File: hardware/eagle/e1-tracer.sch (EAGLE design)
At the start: 108 parts, among them IC1 W25Q80DVSNIG, IC2 MCP1703T-1202E/CB, IC3 TPS73633DCQR, IC4 ASEM1-12.000MHZ-LC-T, J1 PASSTHROUGH, M1 MENTOR_12701001, M2 MENTOR_12701001, T1 BC847C, T2 BC847C, U1 ICE40UP5K-SG48I, U2 IP4234CZ6, U3 IDT82V2081, U4 IDT82V2081, U5 2.048 Mhz, U6 1.544 MHz, X1 MINI-USB-SHIELD-UX60-MB-5ST

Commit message: e1-tracer: finish PCB
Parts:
- removed B1: (no value), microbuilder:SWITCH_TACT_SMT
- removed C15: 10n, rc-sysmocom:CAP_CERAMIC_0603
- removed IC3: TPS73633DCQR, laforge:TPS736XX
- removed JP2: TCLK/MCLK, jumper:JP1E
- removed JP3: 1544/2048, jumper:JP2E
- removed R7: 2.2k, rc-sysmocom:RESISTOR_0402
- added IC5: TLV70233DBVR, tlv700xx:TLV70033-SOT
- added R38: 1k, rc-sysmocom:RESISTOR_0603
- added R39, R40, R41: DNP, rc-sysmocom:RESISTOR_0603
- added SW1: TACTSW-TL3340, tact-switches:TL3340
- added U7: 1.544 MHz, laforge:FOX_FXO-HC73
- added X2: JACK2.5_SJ-2523, laforge:JACK2.5_SJ-2523
- C11: value 1u -> 22u; device rc-sysmocom:CAP_CERAMIC_0603 -> rc-sysmocom:CAP_CERAMIC1206; DESCRIPTION CAP CER 1UF 10V X5R 0603 -> CAP CER 22UF 10V 10% X5R 1206; LINK https://www.digikey.de/product-detail/de/samsung-electro-me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 -> http://www.digikey.de/product-detail/de/foo/1276-1287-1-ND; MANUFACTURER Samsung Electro-Mechanics -> Samsung Electro-Mechanics America, Inc; MANUFACTURERPARTNUMBER CL10A105KP8NNNC -> CL31A226KPHNNNE; SOURCEPARTNUMBER 1276-1182-1-ND -> 1276-1287-1-ND
- C12: value 10n -> 1u; device rc-sysmocom:CAP_CERAMIC_0402 -> rc-sysmocom:CAP_CERAMIC_0603; DESCRIPTION CAP CER 10000PF 25V X7R 0402 -> CAP CER 1UF 10V X5R 0603; LINK https://www.digikey.de/product-detail/de/samsung-electro-mechanics/CL05B103KA5NNNC/1276-1057-1-ND/3889143 -> https://www.digikey.de/product-detail/de/samsung-electro-mechanics/CL10A105KP8NNNC/1276-1182-1-ND/3889268; MANUFACTURERPARTNUMBER CL05B103KA5NNNC -> CL10A105KP8NNNC; SOURCEPARTNUMBER 1276-1057-1-ND -> 1276-1182-1-ND
- C13: value 100n -> 10n; device rc-sysmocom:CAP_CERAMIC_0603 -> rc-sysmocom:CAP_CERAMIC_0402; DESCRIPTION CAP CER 0.1UF 16V 10% X7R 0603 -> CAP CER 10000PF 25V X7R 0402; LINK http://www.digikey.de/product-detail/de/foo/1276-1005-1-ND -> https://www.digikey.de/product-detail/de/samsung-electro-me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; MANUFACTURER Samsung Electro-Mechanics America, Inc -> Samsung Electro-Mechanics; MANUFACTURERPARTNUMBER CL10B104KO8NNNC -> CL05B103KA5NNNC; SOURCEPARTNUMBER 1276-1005-1-ND -> 1276-1057-1-ND
- C14: value 22u -> 100n; device rc-sysmocom:CAP_CERAMIC1206 -> rc-sysmocom:CAP_CERAMIC_0603; DESCRIPTION CAP CER 22UF 10V 10% X5R 1206 -> CAP CER 0.1UF 16V 10% X7R 0603; LINK http://www.digikey.de/product-detail/de/foo/1276-1287-1-ND -> http://www.digikey.de/product-detail/de/foo/1276-1005-1-ND; MANUFACTURERPARTNUMBER CL31A226KPHNNNE -> CL10B104KO8NNNC; SOURCEPARTNUMBER 1276-1287-1-ND -> 1276-1005-1-ND
- IC1: value W25Q80DVSNIG -> MCP1703T-1202E/CB; device spiflash:AT25SF-COMB -> MCP170x:MCP1700; DESCRIPTION IC FLASH 8M SPI 104MHZ 8SOIC -> IC REG LIN 1.2V 200MA SOT23A-3; LINK https://www.digikey.de/product-detail/de/winbond-electronic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 -> https://www.digikey.de/product-detail/de/microchip-technolo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; MANUFACTURER Winbond Electronics -> Microchip Technology; MANUFACTURERPARTNUMBER W25Q80DVSNIG -> MCP1703T-1202E/CB; SOURCEPARTNUMBER W25Q80DVSNIG-ND -> MCP1703T-1202E/CBCT-ND
- IC2: value MCP1703T-1202E/CB -> W25Q80DVSNIG; device MCP170x:MCP1700 -> spiflash:AT25SF-COMB; DESCRIPTION IC REG LIN 1.2V 200MA SOT23A-3 -> IC FLASH 8M SPI 104MHZ 8SOIC; LINK https://www.digikey.de/product-detail/de/microchip-technolo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 -> https://www.digikey.de/product-detail/de/winbond-electronic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; MANUFACTURER Microchip Technology -> Winbond Electronics; MANUFACTURERPARTNUMBER MCP1703T-1202E/CB -> W25Q80DVSNIG; SOURCEPARTNUMBER MCP1703T-1202E/CBCT-ND -> W25Q80DVSNIG-ND
- JP1: CLASS (none) -> CONNECTOR\JUMPER; DESCRIPTION (none) -> NO DESCRIPTION; LINK (none) -> UNKNOWN LINK; MANUFACTURER (none) -> UNKNOWN MANUFACTURER; MANUFACTURERPARTNUMBER (none) -> UNKNOWN MANUFACTURER PART NUMBER; POPULATED (none) -> TRUE; ROHSCERTIFICATE (none) -> UNKNOWN ROHS CERTIFICATE; SOURCE (none) -> UNKNOWN SOURCE; SOURCEPARTNUMBER (none) -> UNKNOWN SOURCE PART NUMBER
- LOS1, LOS2: value RED -> LEDPLCC2-MIN-red; device led:LEDCHIPLED_0805 -> LED-PLCC2:LEDPLCC2-MIN; DESCRIPTION NO DESCRIPTION -> LED RED CLEAR 2PLCC SMD; LINK UNKNOWN LINK -> https://www.digikey.de/product-detail/de/osram-opto-semicon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; MANUFACTURER UNKNOWN MANUFACTURER -> OSRAM Opto Semiconductors Inc.; MANUFACTURERPARTNUMBER UNKNOWN MANUFACTURER PART NUMBER -> LS T676-R1S1-1-Z; SOURCE UNKNOWN SOURCE -> DIGIKEY; SOURCEPARTNUMBER UNKNOWN SOURCE PART NUMBER -> 475-2683-1-ND
- M1, M2: CLASS (none) -> UNKNOWN CLASS; DESCRIPTION (none) -> NO DESCRIPTION; LINK (none) -> UNKNOWN LINK; MANUFACTURER (none) -> UNKNOWN MANUFACTURER; MANUFACTURERPARTNUMBER (none) -> UNKNOWN MANUFACTURER PART NUMBER; POPULATED (none) -> TRUE; ROHSCERTIFICATE (none) -> UNKNOWN ROHS CERTIFICATE; SOURCE (none) -> UNKNOWN SOURCE; SOURCEPARTNUMBER (none) -> UNKNOWN SOURCE PART NUMBER
- PWR: value GREEN -> LEDPLCC2-MIN-green; device led:LEDCHIPLED_0805 -> LED-PLCC2:LEDPLCC2-MIN; CLASS UNKNOWN CLASS -> LED; LINK UNKNOWN LINK -> https://www.digikey.de/product-detail/de/rohm-semiconductor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
- R10: value 10k -> 68
- R28: value 3k 1% -> 10k
- R30: value 10k -> 3k 1%
- R32: value 120 -> 10k
- R34: value 68 -> 120
- R35: value 68 -> 330; DESCRIPTION NO DESCRIPTION -> RES SMD 330 OHM 1%% 1/10W 0603; LINK UNKNOWN LINK -> https://www.digikey.de/product-detail/de/yageo/RC0603FR-073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; MANUFACTURER UNKNOWN MANUFACTURER -> Yageo; MANUFACTURERPARTNUMBER UNKNOWN MANUFACTURER PART NUMBER -> RC0603FR-07330RL; SOURCE UNKNOWN SOURCE -> DIGIKEY; SOURCEPARTNUMBER UNKNOWN SOURCE PART NUMBER -> 311-330HRCT-ND
- R36: value 1k -> 330; DESCRIPTION NO DESCRIPTION -> RES SMD 330 OHM 1%% 1/10W 0603; LINK UNKNOWN LINK -> https://www.digikey.de/product-detail/de/yageo/RC0603FR-073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; MANUFACTURER UNKNOWN MANUFACTURER -> Yageo; MANUFACTURERPARTNUMBER UNKNOWN MANUFACTURER PART NUMBER -> RC0603FR-07330RL; SOURCE UNKNOWN SOURCE -> DIGIKEY; SOURCEPARTNUMBER UNKNOWN SOURCE PART NUMBER -> 311-330HRCT-ND
- R8: value 10k -> 2.2k; device rc-sysmocom:RESISTOR_0603 -> rc-sysmocom:RESISTOR_0402; DESCRIPTION RES 10K OHM 1%% 1/10W 0603 -> RES 2.20K OHM 1/16W 1% 0402 SMD; LINK https://www.digikey.de/product-detail/de/stackpole-electron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 -> http://www.digikey.de/product-detail/de/RC0402FR-072K2L/311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; MANUFACTURER Stackpole Electronics Inc -> Yageo; MANUFACTURERPARTNUMBER YPE HTML PUBLIC -> RC0402FR-072K2L; ROHSCERTIFICATE Bleifrei / RoHS3-konform -> Bleifrei / RoHS-konform; SOURCEPARTNUMBER RMCF0603FT10K0CT-ND -> 311-2.20KLRCT-ND
- R9: value 68 -> 10k; DESCRIPTION NO DESCRIPTION -> RES 10K OHM 1%% 1/10W 0603; LINK UNKNOWN LINK -> https://www.digikey.de/product-detail/de/stackpole-electron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; MANUFACTURER UNKNOWN MANUFACTURER -> Stackpole Electronics Inc; MANUFACTURERPARTNUMBER UNKNOWN MANUFACTURER PART NUMBER -> YPE HTML PUBLIC; ROHSCERTIFICATE UNKNOWN ROHS CERTIFICATE -> Bleifrei / RoHS3-konform; SOURCE UNKNOWN SOURCE -> DIGIKEY; SOURCEPARTNUMBER UNKNOWN SOURCE PART NUMBER -> RMCF0603FT10K0CT-ND
- U3: value IDT82V2081 -> IP4234CZ6; device laforge:IDT82V2081 -> laforge:IP4234CZ6; DESCRIPTION NO DESCRIPTION -> TVS DIODE 5.5V 6TSOP; LINK UNKNOWN LINK -> https://www.digikey.de/product-detail/de/nexperia-usa-inc/I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; MANUFACTURER UNKNOWN MANUFACTURER -> Nexperia USA Inc.; MANUFACTURERPARTNUMBER UNKNOWN MANUFACTURER PART NUMBER -> IP4234CZ6,125; ROHSCERTIFICATE UNKNOWN ROHS CERTIFICATE -> Bleifrei / RoHS-konform; SOURCE UNKNOWN SOURCE -> DIGIKEY; SOURCEPARTNUMBER UNKNOWN SOURCE PART NUMBER -> 1727-4717-1-ND
- U5: value 2.048 Mhz -> IDT82V2081; device laforge:FOX_FXO-HC73 -> laforge:IDT82V2081
- U6: value 1.544 MHz -> 2.048 Mhz; MANUFACTURERPARTNUMBER UNKNOWN MANUFACTURER PART NUMBER -> XLH736002.048000I
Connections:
- removed net N$4 (its old number): R28.2, U3G$5.REF
- new net N$1: R30.2, U5G$5.REF
- new net UART_TX0: U3.1A, X2.MIDDLE
- new net VDD: U3.VCC
- net BOOT_SW: now also SW1.2; no longer B1.P, B1.P1
- net CDONE: now also R8.2; no longer R7.2
- net GND: now also IC5.GND, R18.2, R27.2, R30.1, R40.2, R41.1, SW1.1, SW1.3, U3.GND, U5G$3.!RD/DS/SCLKE, U5G$4.JA0, U5G$4.JA1, U5G$4.MODE1, U5G$4.RCLKE, U5G$4.THZ, U5G$5.GNDA, U5G$5.GNDD, U5G$5.GNDIO, U5G$5.GNDT, U7.GND, X2.RING; no longer B1.S, B1.S1, C15.2, IC3.GND, IC3.GND1, JP3.2, R19.2, R28.1, R9.2, U3G$3.!RD/DS/SCLKE, U3G$4.JA0, U3G$4.JA1, U3G$4.MODE1, U3G$4.RCLKE, U3G$4.THZ, U3G$5.GNDA, U3G$5.GNDD, U3G$5.GNDIO, U3G$5.GNDT, U5.GND
- net IOB_32A_SPI_SO: now also IC2.SO(D1); no longer IC1.SO(D1)
- net IOB_33B_SPI_SI: now also IC2.SI(D0); no longer IC1.SI(D0)
- net IOB_34A_SPI_SCK: now also IC2.SCK; no longer IC1.SCK
- net IOB_35B_SPI_SS: now also IC2.!CS; no longer IC1.!CS
- net IO_A0: now also U5G$3.SDI/WR/RW; no longer U3G$3.SDI/WR/RW
- net IO_A1: now also U5G$3.SDO/!ACK/RDY; no longer U3G$3.SDO/!ACK/RDY
- net IO_A2: now also U5G$3.SCLK/ALE/AS; no longer U3G$3.SCLK/ALE/AS
- net IO_A3: now also U3.1B
- net IO_A4: now also U4G$3.!CS; no longer U3G$3.!CS
- net IO_A5: now also U5G$3.!CS; no longer U4G$3.!CS
- net IO_B0: now also U4G$1.RCLK; no longer U3G$1.RCLK
- net IO_B1: now also U4G$1.RD/RDP; no longer U3G$1.RD/RDP
- net IO_B2: now also U5G$1.RCLK; no longer U4G$1.RCLK
- net IO_B3: now also U5G$1.RD/RDP; no longer U4G$1.RD/RDP
- net LOS0: now also R31.2, U4G$1.LOS; no longer R30.2, U3G$1.LOS
- net LOS1: now also R32.2, U5G$1.LOS; no longer R31.2, U4G$1.LOS
- net MCLK: now also R39.2, U5G$6.MCLK, U7.OUT; no longer JP2.1, U3G$6.MCLK, U5.OUT
- net N$10: now also R13.1, U4G$4.PULS1/AD5; no longer R12.1, U3G$4.PULS1/AD5
- net N$11: now also R14.1, U4G$4.PULS0/AD4; no longer R13.1, U3G$4.PULS0/AD4
- net N$12: now also R15.1, U4G$4.EQ/AD3; no longer R14.1, U3G$4.EQ/AD3
- net N$13: now also R16.1, U4G$4.RPD/AD2; no longer R15.1, U3G$4.RPD/AD2
- net N$14: now also R17.1, U4G$4.PATT1/AD1; no longer R16.1, U3G$4.PATT1/AD1
- net N$15: now also R22.1, U5G$4.PULS1/AD5; no longer R21.1, U4G$4.PULS1/AD5
- net N$16: now also R23.1, U5G$4.PULS0/AD4; no longer R22.1, U4G$4.PULS0/AD4
- net N$17: now also R19.1, U4G$4.!RST; no longer R18.1, U3G$4.!RST
- net N$18: now also R18.1, U4G$4.PATT0/AD0; no longer R17.1, U3G$4.PATT0/AD0
- net N$19: now also R24.1, U5G$4.EQ/AD3; no longer R23.1, U4G$4.EQ/AD3
- net N$2: now also R28.1, U5G$4.!RST; no longer R27.1, U4G$4.!RST
- net N$20: now also R25.1, U5G$4.RPD/AD2; no longer R24.1, U4G$4.RPD/AD2
- net N$21: now also R26.1, U5G$4.PATT1/AD1; no longer R25.1, U4G$4.PATT1/AD1
- net N$22: now also R27.1, U5G$4.PATT0/AD0; no longer R26.1, U4G$4.PATT0/AD0
- net N$23: now also U4G$5.VDDA; no longer U3G$5.VDDA
- net N$25: now also R9.1; no longer R8.1
- net N$26: now also R31.1; no longer R30.1
- net N$27: now also R35.1; no longer R34.1
- net N$28: now also R35.2; no longer R34.2
- net N$29: now also R10.1; no longer R9.1
- net N$3: now also U5G$5.VDDA; no longer U4G$5.VDDA
- net N$30: now also R37.1; no longer R36.1
- net N$31: now also R32.1; no longer R31.1
- net N$35: now also R40.1, U6.E/D; no longer JP3.3, U5.E/D
- net N$36: now also X1S.S2, X1S.S3; no longer C15.1, IC3.NR
- net N$37: now also R36.1; no longer R35.1
- net N$38: now also R41.2, U7.E/D; no longer JP3.1, U6.E/D
- net N$39: now also R36.2; no longer R35.2
- net N$41: now also R38.1; no longer R37.1
- net N$42: now also R37.2; no longer R36.2
- net N$5: now also R38.2; no longer R37.2
- net N$6: now also R20.1, U5G$4.PULS3/AD7; no longer R19.1, U4G$4.PULS3/AD7
- net N$61: now also C13.1; no longer C12.1
- net N$7: now also R21.1, U5G$4.PULS2/AD6; no longer R20.1, U4G$4.PULS2/AD6
- net N$8: now also R11.1, U4G$4.PULS3/AD7; no longer R10.1, U3G$4.PULS3/AD7
- net N$9: now also R12.1, U4G$4.PULS2/AD6; no longer R11.1, U3G$4.PULS2/AD6
- net RRING: now also R33.1, U4G$2.RRING; no longer R32.1, U3G$2.RRING
- net RRING1: now also R34.1, U5G$2.RRING; no longer R33.1, U4G$2.RRING
- net RTIP: now also R33.2, U4G$2.RTIP; no longer R32.2, U3G$2.RTIP
- net RTIP1: now also R34.2, U5G$2.RTIP; no longer R33.2, U4G$2.RTIP
- net TCLK: now also R39.1, U5G$1.TCLK; no longer JP2.2, U3G$1.TCLK
- net VBUS: now also C11.1, C12.1, IC1.VIN, IC5.IN; no longer C10.1, C14.1, IC2.VIN, IC3.IN
- net VCC_1V2: now also C10.1, IC1.VO, IC5.EN; no longer C11.1, IC2.VO, IC3.EN
- net VCC_3V3: now also C14.1, IC2.!HOLD(D3), IC2.!WP(D2), IC2.VCC, IC5.OUT, R19.2, R28.2, R8.1, R9.2, U5G$4.MODE0, U5G$5.VDDD, U5G$5.VDDIO, U5G$5.VDDT, U7.VCC; no longer C13.1, IC1.!HOLD(D3), IC1.!WP(D2), IC1.VCC, IC3.OUT, R18.2, R27.2, R7.1, R8.2, U3G$4.MODE0, U3G$5.VDDD, U3G$5.VDDIO, U3G$5.VDDT, U5.VCC
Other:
- note added: "Osmocom-style 3.3V UART on 2.5mm jack"
- note added: "serial debug out"
- moved on the sheet: C10, C11, C12, C13, C14, C16, C29, C9, R11, R12, R13, R14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

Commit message: e1-tracer: reapir missing VDD_3V3 on serial debug out's TVS
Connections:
- removed net VDD: U3.VCC
- net VCC_3V3: now also U3.VCC
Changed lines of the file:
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@@
 </part>
 <part name="GND42" library="supply1" deviceset="GND" device=""/>
-<part name="VDD1" library="supply1" deviceset="VDD" device=""/>
 <part name="IC5" library="tlv700xx" deviceset="TLV700*" device="-SOT" technology="33" value="TLV70233DBVR">
 <attribute name="OC_DIGIKEY" value="296-32415-1-ND"/>
@@
 </instance>
 <instance part="GND42" gate="1" x="314.96" y="193.04"/>
-<instance part="VDD1" gate="G$1" x="314.96" y="226.06"/>
 <instance part="IC5" gate="G$1" x="238.76" y="213.36"/>
 </instances>
@@
 <label x="187.96" y="25.4" size="1.27" layer="95" rot="R90" xref="yes"/>
 </segment>
+<segment>
+<pinref part="U3" gate="G$1" pin="VCC"/>
+<wire x1="314.96" y1="215.9" x2="314.96" y2="218.44" width="0.1524" layer="91"/>
+<label x="314.96" y="218.44" size="1.27" layer="95" rot="R90" xref="yes"/>
+</segment>
 </net>
 <net name="VBUS" class="1">
@@
 </segment>
 </net>
-<net name="VDD" class="2">
-<segment>
-<pinref part="U3" gate="G$1" pin="VCC"/>
-<wire x1="314.96" y1="215.9" x2="314.96" y2="223.52" width="0.1524" layer="91"/>
-<pinref part="VDD1" gate="G$1" pin="VDD"/>
-</segment>
-</net>

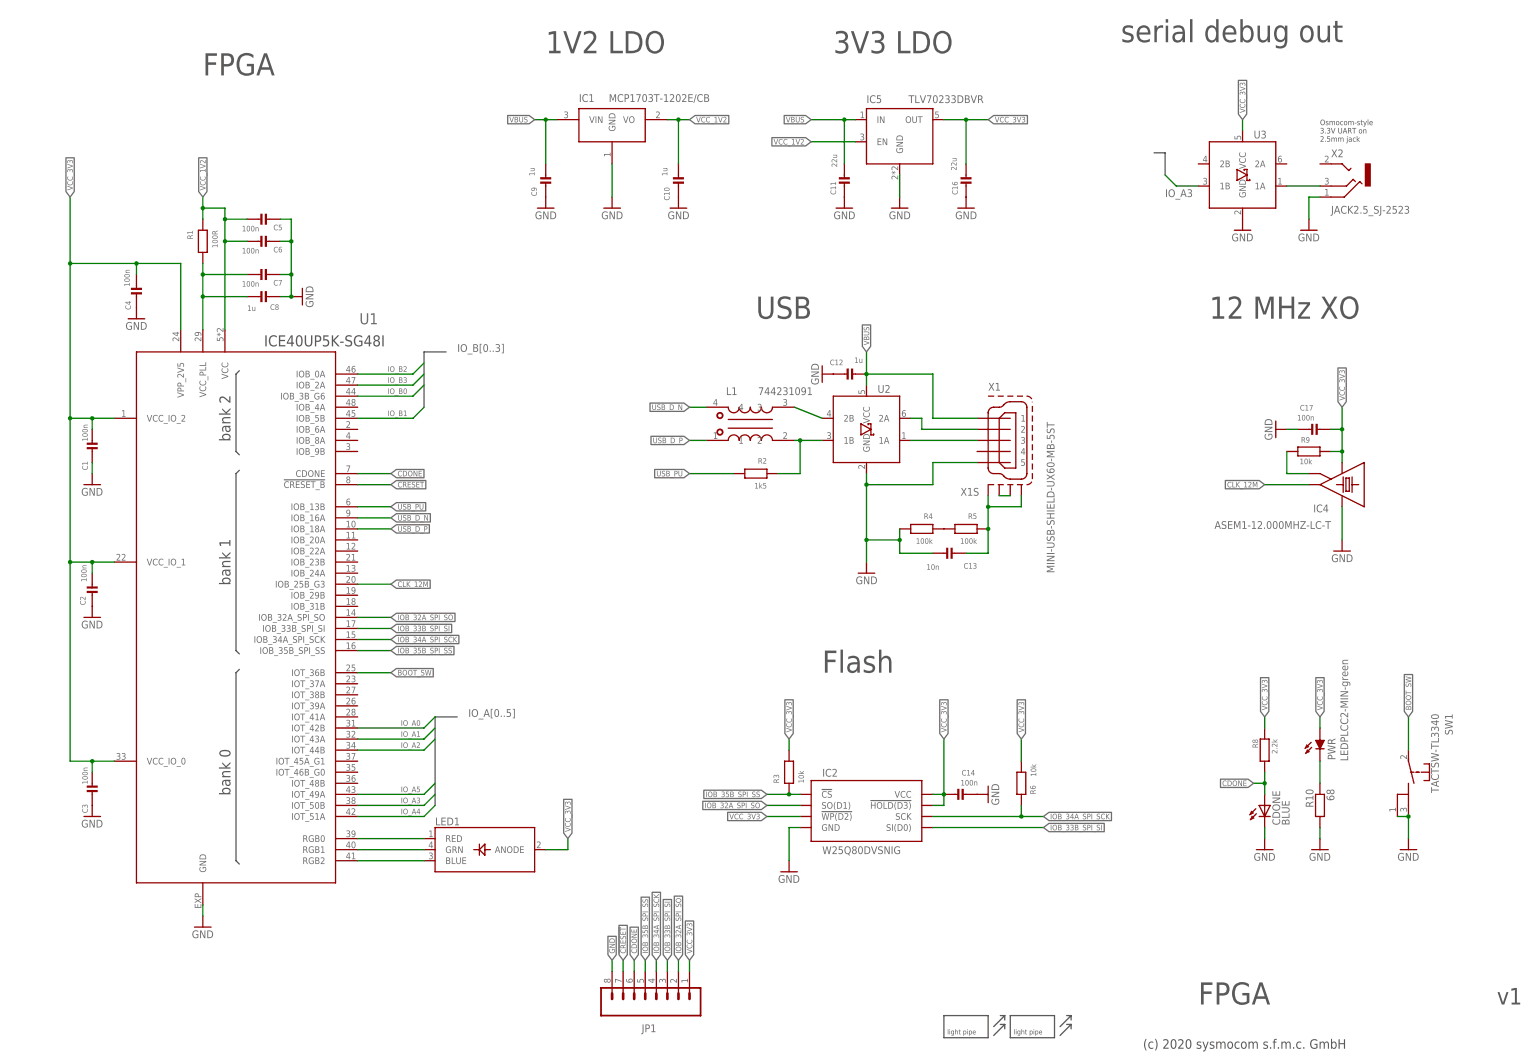
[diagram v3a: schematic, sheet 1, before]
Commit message: e1-tracer: add 2x 33R series resistors in USB wires
and
* update improved HC73 package
* move upper third of PCB (LIUs and XOs) left
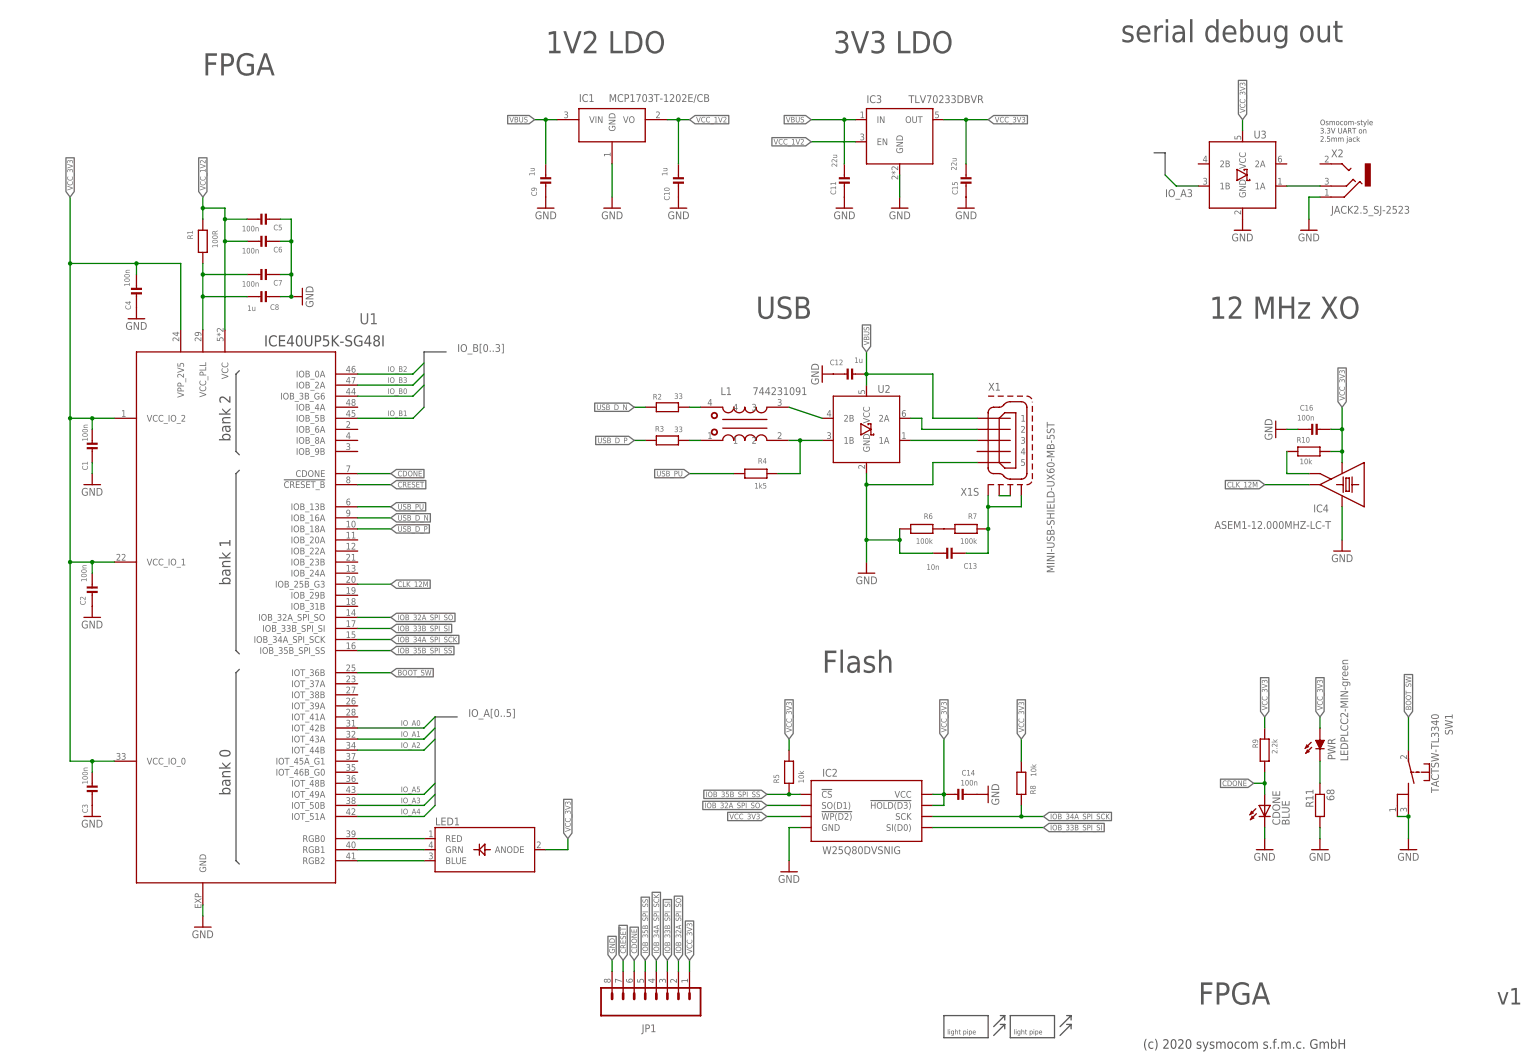
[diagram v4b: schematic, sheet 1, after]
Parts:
- removed C29: 100n, rc-sysmocom:CAP_CERAMIC_0603
- added C15: 22u, rc-sysmocom:CAP_CERAMIC1206
- added R42: DNP, rc-sysmocom:RESISTOR_0603
- added R7: 100k, rc-sysmocom:RESISTOR_0603
- C16: value 22u -> 100n; device rc-sysmocom:CAP_CERAMIC1206 -> rc-sysmocom:CAP_CERAMIC_0603; DESCRIPTION CAP CER 22UF 10V 10% X5R 1206 -> CAP CER 0.1UF 16V 10% X7R 0603; LINK http://www.digikey.de/product-detail/de/foo/1276-1287-1-ND -> http://www.digikey.de/product-detail/de/foo/1276-1005-1-ND; MANUFACTURERPARTNUMBER CL31A226KPHNNNE -> CL10B104KO8NNNC; SOURCEPARTNUMBER 1276-1287-1-ND -> 1276-1005-1-ND
- C17: value 100n -> 68µ DNP
- C19: value 68µ DNP -> 100n
- R10: value 68 -> 10k; DESCRIPTION NO DESCRIPTION -> RES 10K OHM 1%% 1/10W 0603; LINK UNKNOWN LINK -> https://www.digikey.de/product-detail/de/stackpole-electron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; MANUFACTURER UNKNOWN MANUFACTURER -> Stackpole Electronics Inc; MANUFACTURERPARTNUMBER UNKNOWN MANUFACTURER PART NUMBER -> YPE HTML PUBLIC; ROHSCERTIFICATE UNKNOWN ROHS CERTIFICATE -> Bleifrei / RoHS3-konform; SOURCE UNKNOWN SOURCE -> DIGIKEY; SOURCEPARTNUMBER UNKNOWN SOURCE PART NUMBER -> RMCF0603FT10K0CT-ND
- R11: value 10k -> 68
- R2: value 1k5 -> 33; device rc-sysmocom:RESISTOR_0603 -> rc-sysmocom:RESISTOR_0402
- R29: value 3k 1% -> 10k
- R3: value 10k -> 33; device rc-sysmocom:RESISTOR_0603 -> rc-sysmocom:RESISTOR_0402; DESCRIPTION RES 10K OHM 1%% 1/10W 0603 -> NO DESCRIPTION; LINK https://www.digikey.de/product-detail/de/stackpole-electron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 -> UNKNOWN LINK; MANUFACTURER Stackpole Electronics Inc -> UNKNOWN MANUFACTURER; MANUFACTURERPARTNUMBER YPE HTML PUBLIC -> UNKNOWN MANUFACTURER PART NUMBER; ROHSCERTIFICATE Bleifrei / RoHS3-konform -> UNKNOWN ROHS CERTIFICATE; SOURCE DIGIKEY -> UNKNOWN SOURCE; SOURCEPARTNUMBER RMCF0603FT10K0CT-ND -> UNKNOWN SOURCE PART NUMBER
- R31: value 10k -> 3k 1%
- R33: value 120 -> 10k
- R35: value 330 -> 120; DESCRIPTION RES SMD 330 OHM 1%% 1/10W 0603 -> NO DESCRIPTION; LINK https://www.digikey.de/product-detail/de/yageo/RC0603FR-073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 -> UNKNOWN LINK; MANUFACTURER Yageo -> UNKNOWN MANUFACTURER; MANUFACTURERPARTNUMBER RC0603FR-07330RL -> UNKNOWN MANUFACTURER PART NUMBER; SOURCE DIGIKEY -> UNKNOWN SOURCE; SOURCEPARTNUMBER 311-330HRCT-ND -> UNKNOWN SOURCE PART NUMBER
- R37: value 1k -> 330; DESCRIPTION NO DESCRIPTION -> RES SMD 330 OHM 1%% 1/10W 0603; LINK UNKNOWN LINK -> https://www.digikey.de/product-detail/de/yageo/RC0603FR-073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; MANUFACTURER UNKNOWN MANUFACTURER -> Yageo; MANUFACTURERPARTNUMBER UNKNOWN MANUFACTURER PART NUMBER -> RC0603FR-07330RL; SOURCE UNKNOWN SOURCE -> DIGIKEY; SOURCEPARTNUMBER UNKNOWN SOURCE PART NUMBER -> 311-330HRCT-ND
- R39: value DNP -> 1k; DESCRIPTION RES SMD 0 OHM JUMPER 1/10W 0603 -> NO DESCRIPTION; LINK https://www.digikey.de/product-detail/de/panasonic-electron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 -> UNKNOWN LINK; MANUFACTURER Panasonic Electronic Components -> UNKNOWN MANUFACTURER; MANUFACTURERPARTNUMBER ERJ-3GEY0R00V -> UNKNOWN MANUFACTURER PART NUMBER; SOURCE DIGIKEY -> UNKNOWN SOURCE; SOURCEPARTNUMBER P0.0GCT-ND -> UNKNOWN SOURCE PART NUMBER
- R4: value 100k -> 1k5; DESCRIPTION RES SMD 100K OHM 5%% 1/10W 0603 -> NO DESCRIPTION; LINK https://www.digikey.de/product-detail/de/yageo/RC0603JR-071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 -> UNKNOWN LINK; MANUFACTURER Yageo -> UNKNOWN MANUFACTURER; MANUFACTURERPARTNUMBER RC0603JR-07100KL -> UNKNOWN MANUFACTURER PART NUMBER; ROHSCERTIFICATE Bleifrei / RoHS-konform -> UNKNOWN ROHS CERTIFICATE; SOURCE DIGIKEY -> UNKNOWN SOURCE; SOURCEPARTNUMBER 311-100KGRCT-ND -> UNKNOWN SOURCE PART NUMBER
- R5: value 100k -> 10k; DESCRIPTION RES SMD 100K OHM 5%% 1/10W 0603 -> RES 10K OHM 1%% 1/10W 0603; LINK https://www.digikey.de/product-detail/de/yageo/RC0603JR-071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 -> https://www.digikey.de/product-detail/de/stackpole-electron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; MANUFACTURER Yageo -> Stackpole Electronics Inc; MANUFACTURERPARTNUMBER RC0603JR-07100KL -> YPE HTML PUBLIC; ROHSCERTIFICATE Bleifrei / RoHS-konform -> Bleifrei / RoHS3-konform; SOURCEPARTNUMBER 311-100KGRCT-ND -> RMCF0603FT10K0CT-ND
- R6: value 10k -> 100k; DESCRIPTION RES 10K OHM 1%% 1/10W 0603 -> RES SMD 100K OHM 5%% 1/10W 0603; LINK https://www.digikey.de/product-detail/de/stackpole-electron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 -> https://www.digikey.de/product-detail/de/yageo/RC0603JR-071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; MANUFACTURER Stackpole Electronics Inc -> Yageo; MANUFACTURERPARTNUMBER RMCF0603FT10K0 -> RC0603JR-07100KL; ROHSCERTIFICATE UNKNOWN ROHS CERTIFICATE -> Bleifrei / RoHS-konform; SOURCEPARTNUMBER RMCF0603FT10K0CT-ND -> 311-100KGRCT-ND
- R8: value 2.2k -> 10k; device rc-sysmocom:RESISTOR_0402 -> rc-sysmocom:RESISTOR_0603; DESCRIPTION RES 2.20K OHM 1/16W 1% 0402 SMD -> RES 10K OHM 1%% 1/10W 0603; LINK http://www.digikey.de/product-detail/de/RC0402FR-072K2L/311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 -> https://www.digikey.de/product-detail/de/stackpole-electron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; MANUFACTURER Yageo -> Stackpole Electronics Inc; MANUFACTURERPARTNUMBER RC0402FR-072K2L -> RMCF0603FT10K0; ROHSCERTIFICATE Bleifrei / RoHS-konform -> UNKNOWN ROHS CERTIFICATE; SOURCEPARTNUMBER 311-2.20KLRCT-ND -> RMCF0603FT10K0CT-ND
- R9: value 10k -> 2.2k; device rc-sysmocom:RESISTOR_0603 -> rc-sysmocom:RESISTOR_0402; DESCRIPTION RES 10K OHM 1%% 1/10W 0603 -> RES 2.20K OHM 1/16W 1% 0402 SMD; LINK https://www.digikey.de/product-detail/de/stackpole-electron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 -> http://www.digikey.de/product-detail/de/RC0402FR-072K2L/311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; MANUFACTURER Stackpole Electronics Inc -> Yageo; MANUFACTURERPARTNUMBER YPE HTML PUBLIC -> RC0402FR-072K2L; ROHSCERTIFICATE Bleifrei / RoHS3-konform -> Bleifrei / RoHS-konform; SOURCEPARTNUMBER RMCF0603FT10K0CT-ND -> 311-2.20KLRCT-ND
- renumbered IC5 to IC3
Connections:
- new net _D_N: L1.4, R2.2
- new net _D_P: L1.1, R3.2
- net CDONE: now also R9.2; no longer R8.2
- net GND: now also C15.2, C17.1, C19.2, C27.1, R19.2, R28.2, R31.1, R41.2, R42.1, R6.1; no longer C17.2, C19.1, C27.2, C29.1, R10.2, R20.2, R29.1, R4.1, R40.2, R41.1
- net IOB_34A_SPI_SCK: now also R8.1; no longer R6.1
- net IOB_35B_SPI_SS: now also R5.1; no longer R3.1
- net LOS0: now also R32.2; no longer R31.2
- net LOS1: now also R33.2; no longer R32.2
- net MCLK: now also R40.2; no longer R39.2
- net N$1: now also R31.2; no longer R30.2
- net N$10: now also R14.1; no longer R13.1
- net N$11: now also R15.1; no longer R14.1
- net N$12: now also R16.1; no longer R15.1
- net N$13: now also R17.1; no longer R16.1
- net N$14: now also R18.1; no longer R17.1
- net N$15: now also R23.1; no longer R22.1
- net N$16: now also R24.1; no longer R23.1
- net N$17: now also R20.1; no longer R19.1
- net N$18: now also R19.1; no longer R18.1
- net N$19: now also R25.1; no longer R24.1
- net N$2: now also R29.1; no longer R28.1
- net N$20: now also R26.1; no longer R25.1
- net N$21: now also R27.1; no longer R26.1
- net N$22: now also R28.1; no longer R27.1
- net N$23: now also C25.1; no longer C26.1
- net N$25: now also R10.1; no longer R9.1
- net N$26: now also R32.1; no longer R31.1
- net N$27: now also R36.1; no longer R35.1
- net N$28: now also R36.2; no longer R35.2
- net N$29: now also R11.1; no longer R10.1
- net N$3: now also C26.1; no longer C27.1
- net N$30: now also R38.1; no longer R37.1
- net N$31: now also R33.1; no longer R32.1
- net N$35: now also R41.1; no longer R40.1
- net N$37: now also R37.1; no longer R36.1
- net N$38: now also R42.2; no longer R41.2
- net N$39: now also R37.2; no longer R36.2
- net N$4: now also R30.2; no longer R29.2
- net N$41: now also R39.1; no longer R38.1
- net N$42: now also R38.2; no longer R37.2
- net N$5: now also R39.2; no longer R38.2
- net N$55: now also R6.2, R7.1; no longer R4.2, R5.1
- net N$6: now also R21.1; no longer R20.1
- net N$61: now also R7.2; no longer R5.2
- net N$7: now also R22.1; no longer R21.1
- net N$8: now also R12.1; no longer R11.1
- net N$9: now also R13.1; no longer R12.1
- net RRING: now also R34.1; no longer R33.1
- net RRING1: now also R35.1; no longer R34.1
- net RTIP: now also R34.2; no longer R33.2
- net RTIP1: now also R35.2; no longer R34.2
- net TCLK: now also R40.1; no longer R39.1
- net USB1_D_P: now also R4.2; no longer R2.2
- net USB_D_N: now also R2.1; no longer L1.4
- net USB_D_P: now also R3.1; no longer L1.1
- net USB_PU: now also R4.1; no longer R2.1
- net VCC_3V3: now also C15.1, C17.2, C19.1, C27.2, R10.2, R20.2, R29.2, R5.2, R8.2, R9.1; no longer C17.1, C19.2, C25.1, C29.2, R19.2, R28.2, R3.2, R6.2, R8.1, R9.2
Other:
- moved on the sheet: C16, C18, C19, C20, C21, C22, C23, C24, C25, C26, C27, C28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
